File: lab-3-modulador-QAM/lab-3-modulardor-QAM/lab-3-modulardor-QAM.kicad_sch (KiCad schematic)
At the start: 58 parts, among them J1 señales I-Q, J3 Fuente, Q1 2N3904, U1 LM741, U4 MC1496, U5 MC1496, U6 LM741, U7 LM358

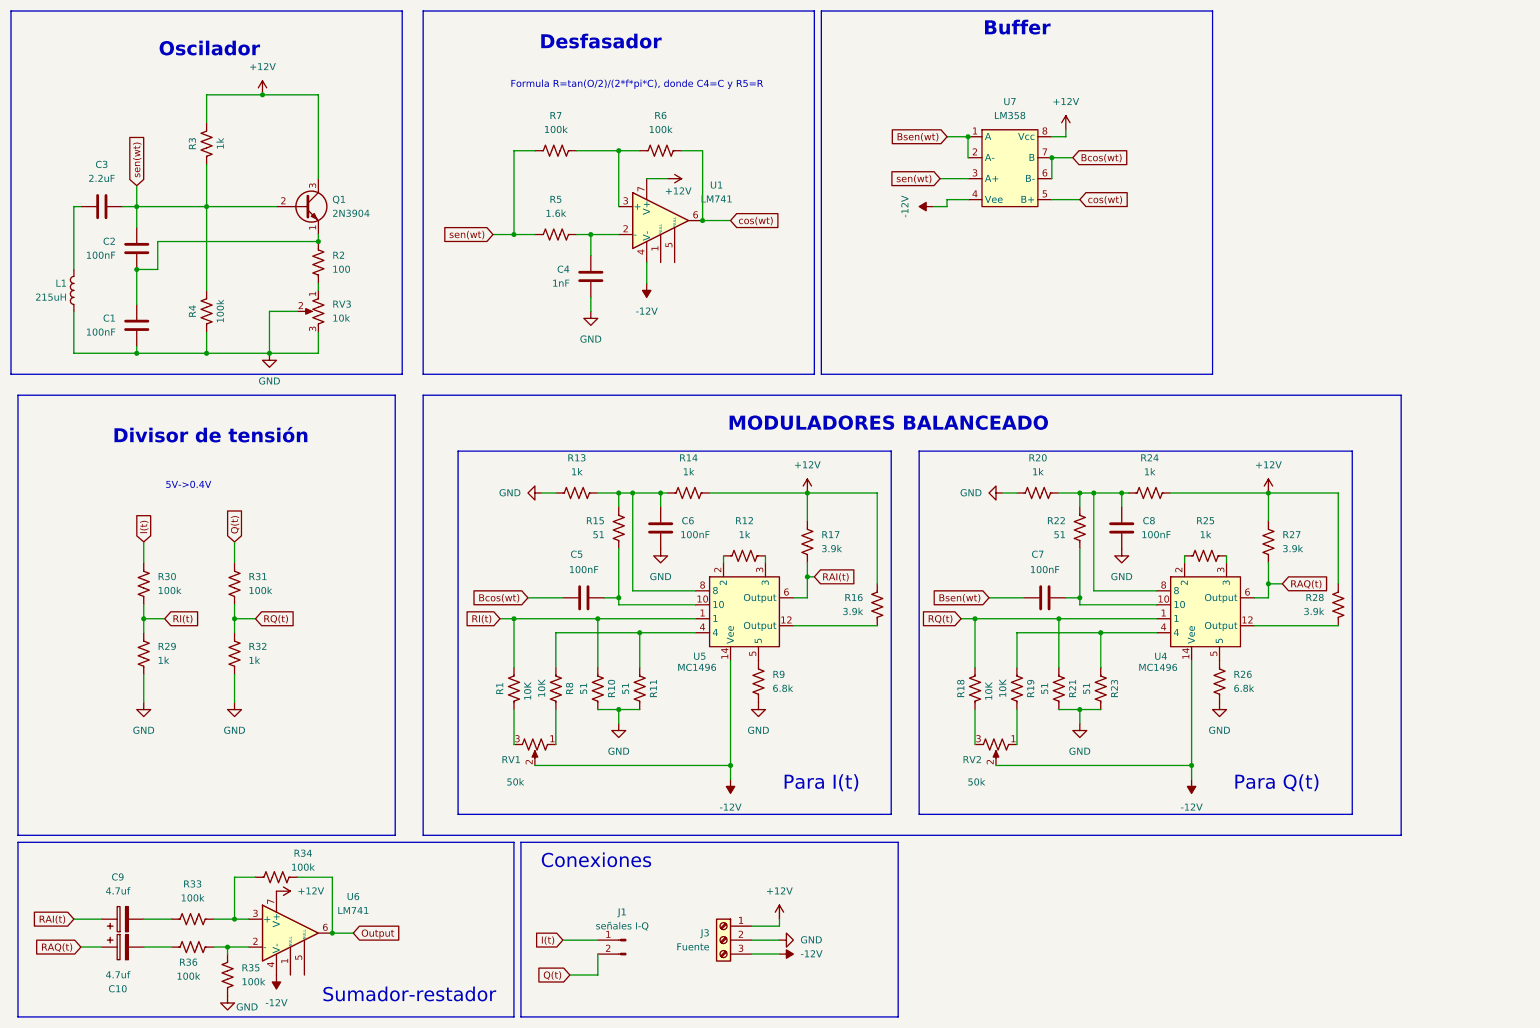
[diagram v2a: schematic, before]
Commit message: Separadando por partes. Oscilador y Modulador
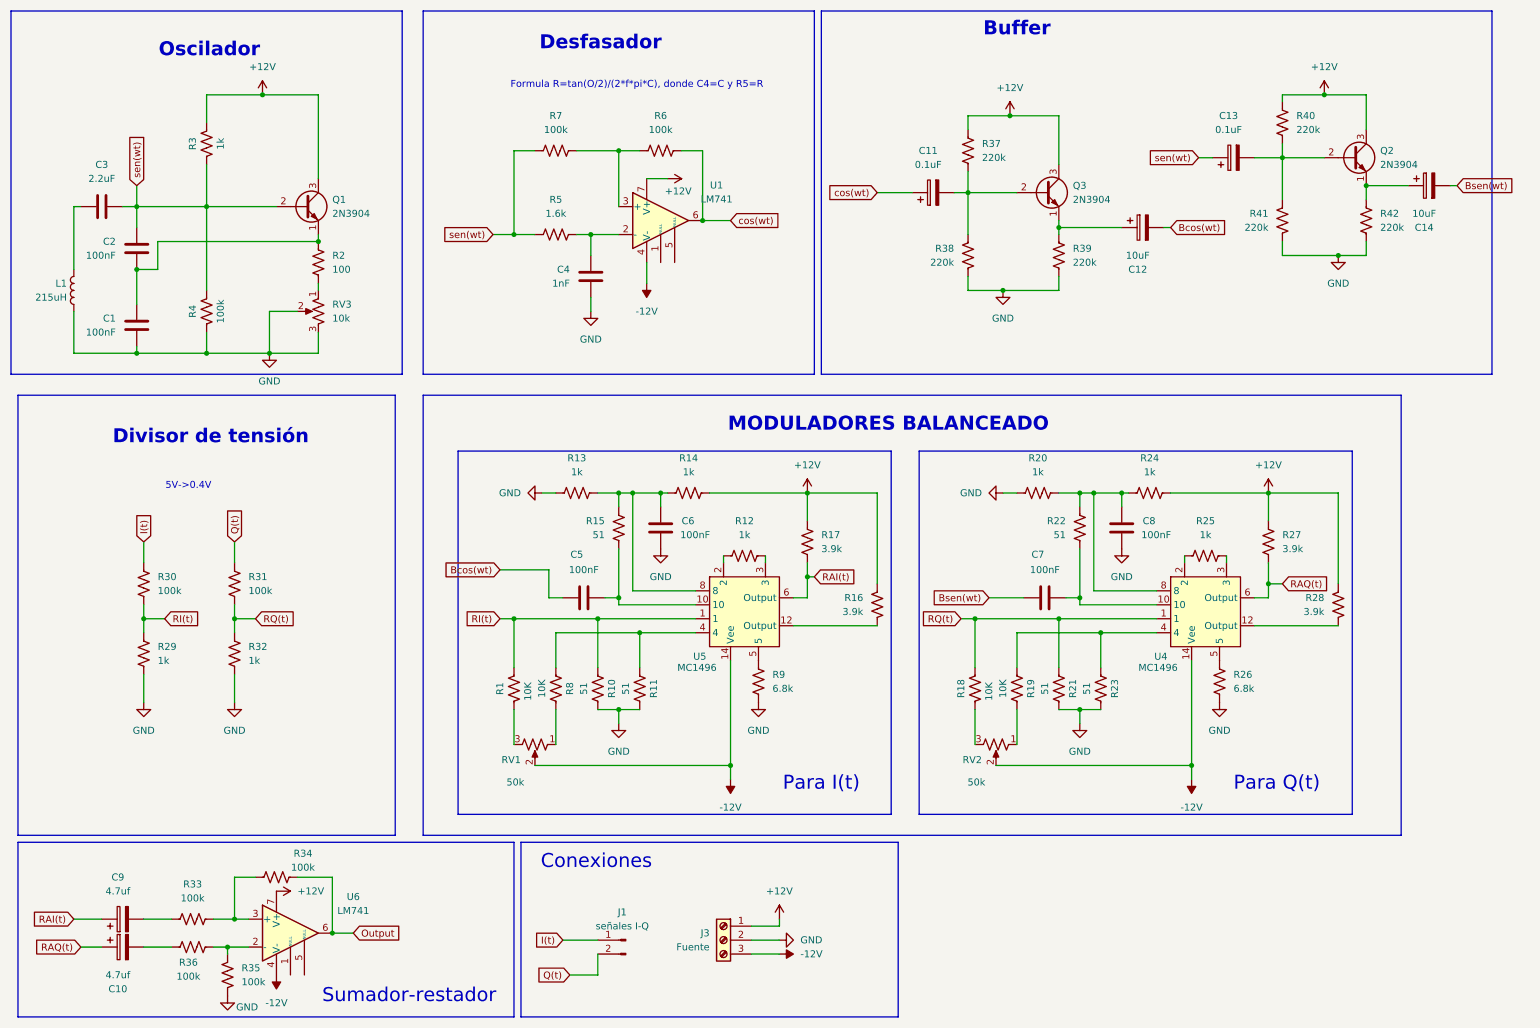
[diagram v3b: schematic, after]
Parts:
- removed U7: LM358, Package_DIP:DIP-8_W10.16mm, symbol otros_componentes:LM358
- added C11, C13: 0.1uF, Capacitor_THT:CP_Radial_D4.0mm_P1.50mm, symbol Device:C_Polarized
- added C12, C14: 10uF, Capacitor_THT:CP_Radial_D4.0mm_P1.50mm, symbol Device:C_Polarized
- added Q2, Q3: 2N3904, Package_TO_SOT_THT:TO-92_Inline, symbol Transistor_BJT:2N3904
- added R37, R38, R39, R40, R41, R42: 220k, Resistor_THT:R_Axial_DIN0309_L9.0mm_D3.2mm_P12.70mm_Horizontal, symbol Device:R_US
- L1: footprint Inductor_THT:L_Axial_L5.3mm_D2.2mm_P2.54mm_Vertical_Vishay_IM-1 -> Inductor_THT:L_Axial_L6.6mm_D2.7mm_P10.16mm_Horizontal_Vishay_IM-2
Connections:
- net +12V: now also Q2.3 (C), Q3.3 (C), R37.1, R40.1
- net Bcos(wt): now also C12.2
- net Bsen(wt): now also C14.2
- net GND: now also R38.2, R39.2, R41.2, R42.2
- net cos(wt): now also C11.1
- net sen(wt): now also C13.1
- new net: C11.2, Q3.2 (B), R37.2, R38.1
- new net: C14.1, Q2.1 (E), R42.1
- new net: C13.2, Q2.2 (B), R40.2, R41.1
- new net: C12.1, Q3.1 (E), R39.1

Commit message: Diseño final de modulador 8QAM
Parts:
- removed R30, R31: 100k, Resistor_THT:R_Axial_DIN0309_L9.0mm_D3.2mm_P12.70mm_Horizontal, symbol Device:R_US
- added Q4, Q5: 2N3904, Package_TO_SOT_THT:TO-92_Inline, symbol Transistor_BJT:2N3904
- R32: value 1k -> 10k
- R39, R42: value 220k -> 10k
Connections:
- net I(t): now also Q5.2 (B)
- net Q(t): now also Q4.2 (B)
- net RI(t): now also Q5.1 (E)
- net RQ(t): now also Q4.1 (E)
- new net +5V: Q4.3 (C), Q5.3 (C)
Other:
- moved on the sheet: R32
